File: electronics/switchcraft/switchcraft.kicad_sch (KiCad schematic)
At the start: 1 part

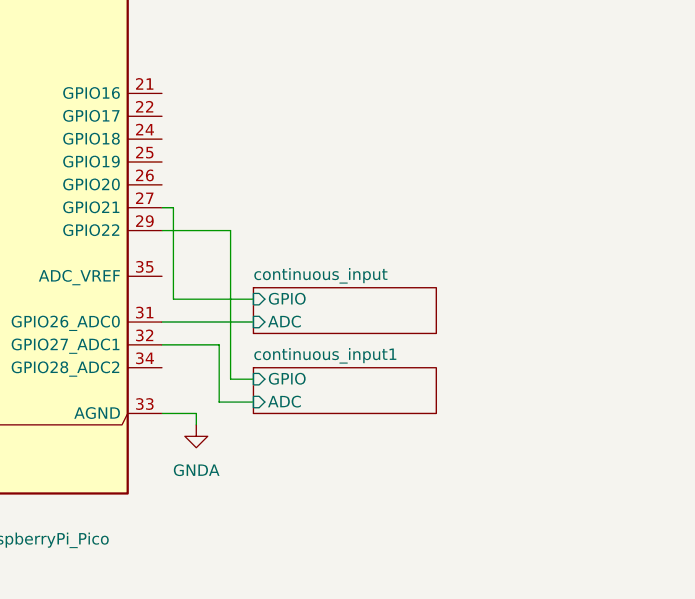
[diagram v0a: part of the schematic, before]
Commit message: simplified continuous inputs
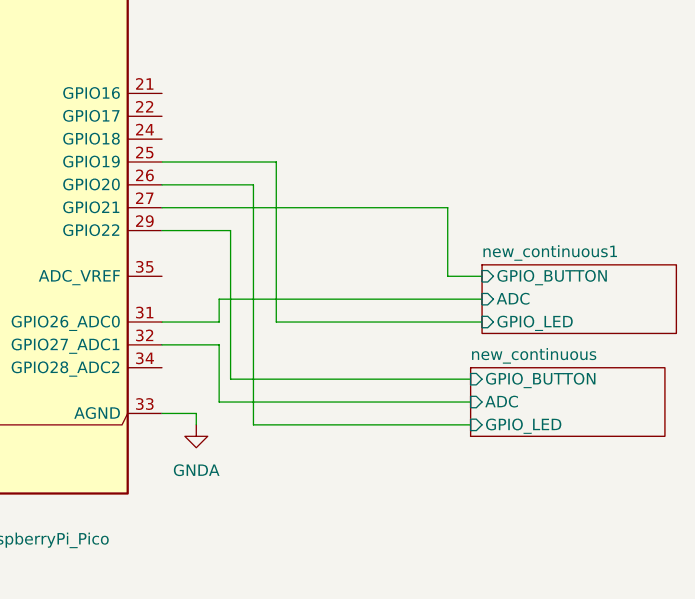
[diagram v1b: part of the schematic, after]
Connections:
- net new_continuous1/GPIO_LED: now reaches A1.25 (GPIO19)
- net new_continuous/GPIO_LED: now reaches A1.26 (GPIO20)
- net continuous_input/ADC renamed new_continuous1/ADC
- net continuous_input/GPIO renamed new_continuous1/GPIO_BUTTON
- net continuous_input1/ADC renamed new_continuous/ADC
- net continuous_input1/GPIO renamed new_continuous/GPIO_BUTTON
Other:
- removed sheet continuous_input
- removed sheet continuous_input1
- added sheet new_continuous (new_continuous.kicad_sch)
- added sheet new_continuous1 (new_continuous.kicad_sch)
